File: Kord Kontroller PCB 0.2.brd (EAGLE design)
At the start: 242.5 x 100 mm, 188 parts, among them IC2 74HCT1G125DBV, J1 MIDIOUTB, J2 MIDIOUTA, J3 FTSH-105-01-L-DV-KJ, SW2 SPST_TACT-KMR2, U1 AP2112K-3.3, U2 ATSAMD51J19A-AUT, X3 microUSB

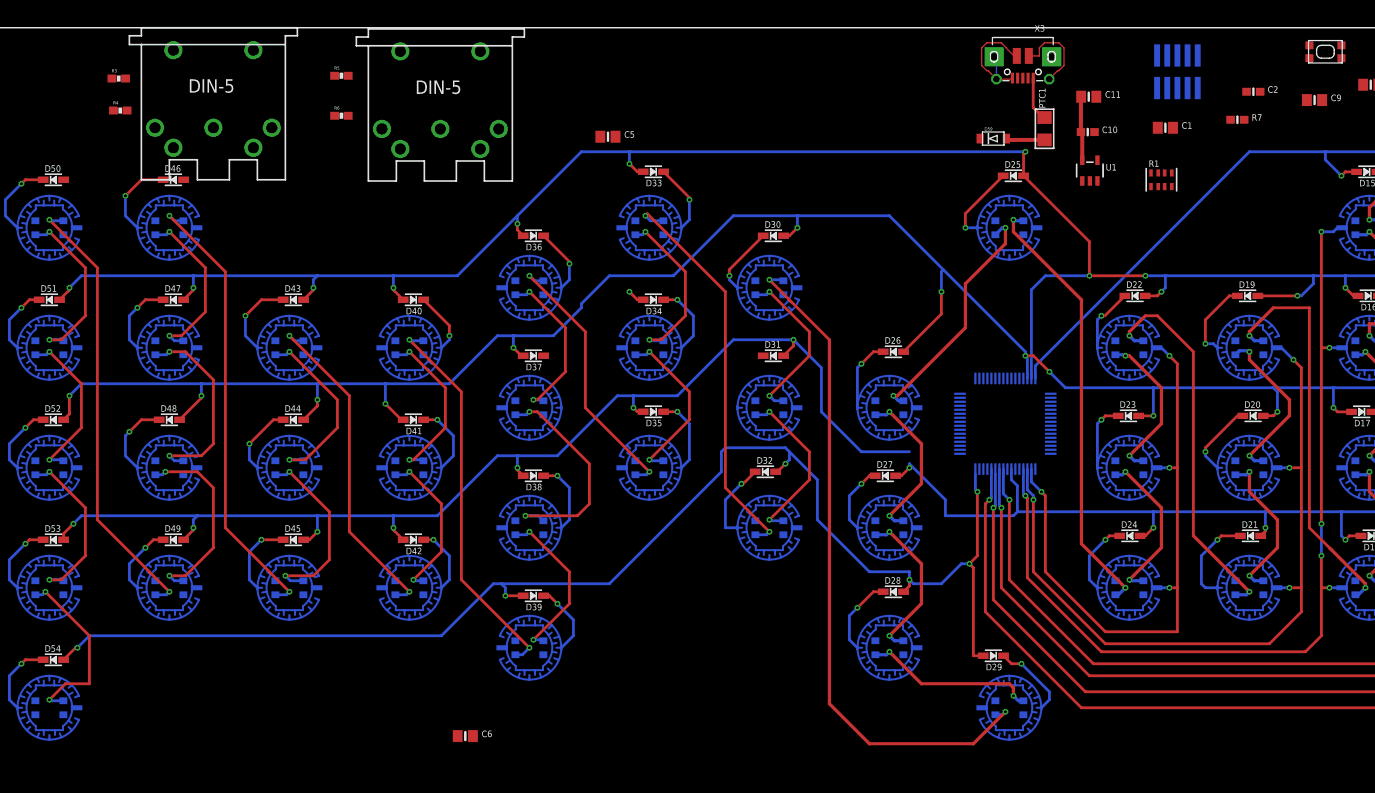
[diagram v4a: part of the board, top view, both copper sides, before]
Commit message: Added traces for 7-14
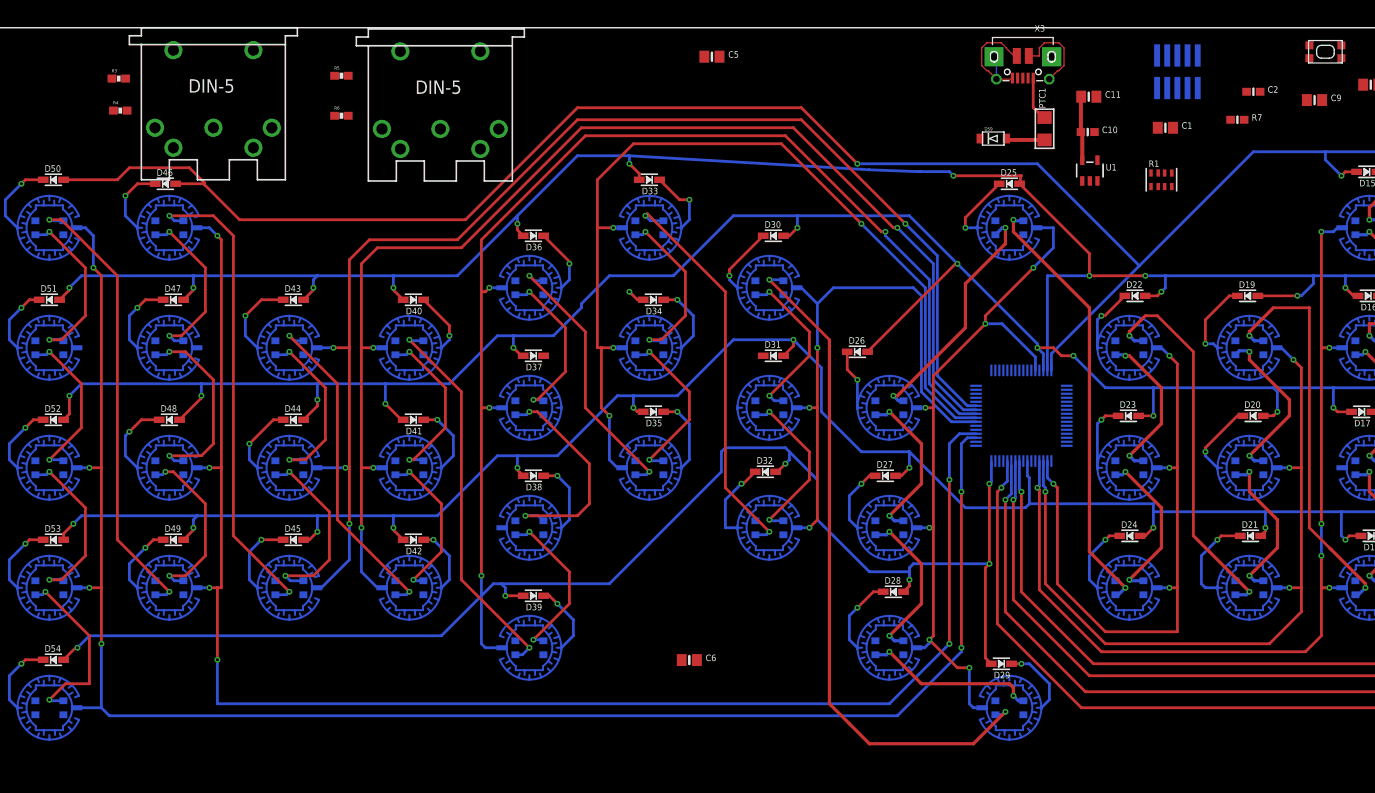
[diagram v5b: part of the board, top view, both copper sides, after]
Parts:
- moved C6 29.6 mm to (87.5, 21.0)
- moved C5 16.4 mm to (90.3, 96.4)
- moved D26 4.50 mm to (108.5, 59.5)
- moved U2 2.24 mm to (129.0, 51.5)
- moved D29 1.41 mm to (126.5, 20.5)
- moved D25 1.12 mm to (127.5, 80.5)
- moved D33 1.12 mm to (82.5, 81.0)
- moved D46 1.12 mm to (22.0, 80.5)
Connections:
- net COL10: now also U2.41; no longer U2.38
- net COL11: now also U2.42; no longer U2.41
- net COL12: now also U2.37, U2.43; no longer U2.42
- net COL13: now also U2.36; no longer U2.43
- net COL14: now also U2.35; no longer U2.44
- net COL7: now also B29.P$1, U2.60; no longer U2.35
- net COL8: now also U2.39; no longer B29.P$1, U2.36
- net COL9: now also U2.40; no longer U2.37
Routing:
- net COL14: track 0.00 -> 210.0 mm, vias 0 -> 6
- net COL13: track 0.00 -> 190.8 mm, vias 0 -> 6
- net COL12: track 0.00 -> 159.8 mm, vias 0 -> 4
- net COL11: track 0.00 -> 153.5 mm, vias 0 -> 4
- net ROW0: track 104.2 -> 257.7 mm, vias 3 -> 4
- net COL10: track 0.00 -> 148.2 mm, vias 0 -> 4
- net COL9: track 0.00 -> 113.7 mm, vias 0 -> 4
- net COL7: track 0.00 -> 88.3 mm, vias 0 -> 6
- net COL8: track 0.00 -> 70.1 mm, vias 0 -> 3
- net ROW1: track 312.9 -> 308.1 mm
- net ROW4: track 171.1 -> 175.2 mm
- net ROW2: track 316.4 -> 320.2 mm
- net N$100: track 57.1 -> 60.3 mm
- net N$112: track 24.7 -> 22.1 mm
- net N$81: track 9.06 -> 7.53 mm
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
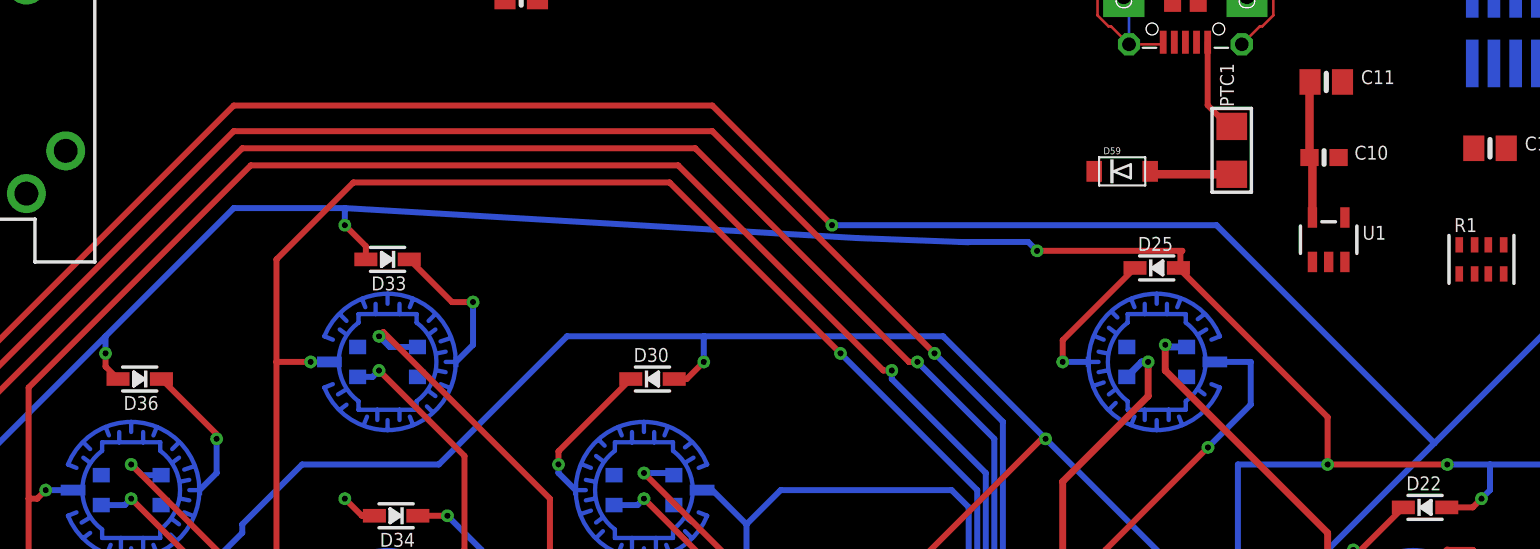
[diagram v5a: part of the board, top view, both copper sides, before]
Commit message: added last top button diodes
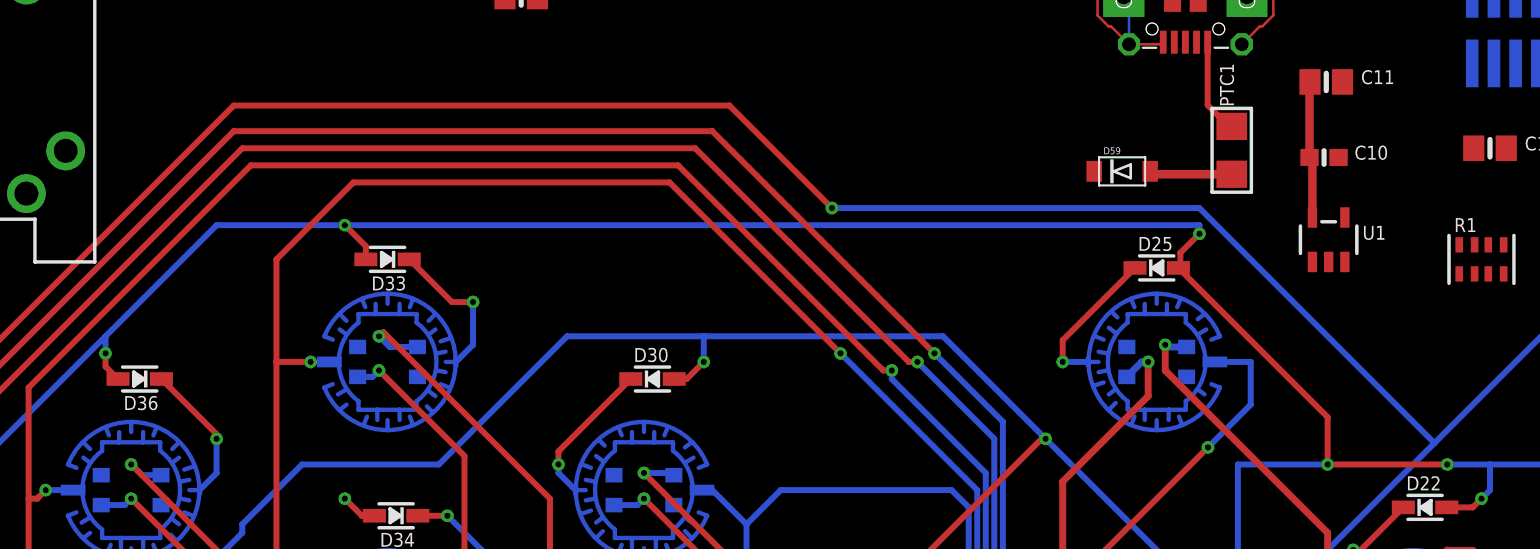
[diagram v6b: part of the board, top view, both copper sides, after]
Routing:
- net ROW1: track 308.1 -> 308.8 mm
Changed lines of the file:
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@@
 <wire x1="41" y1="69" x2="25.5" y2="69" width="0.35" layer="16"/>
 <wire x1="25.5" y1="69" x2="11.5" y2="69" width="0.35" layer="16"/>
-<wire x1="73.5" y1="84" x2="80" y2="84" width="0.35" layer="16"/>
-<wire x1="80" y1="84" x2="109.986528125" y2="82.2458375" width="0.35" layer="16"/>
-<wire x1="109.986528125" y1="82.2458375" x2="116.0007125" y2="82.01884375" width="0.35" layer="16"/>
-<wire x1="116.0007125" y1="82.01884375" x2="116.5" y2="82" width="0.35" layer="16"/>
+<wire x1="80" y1="83" x2="72.5" y2="83" width="0.35" layer="16"/>
+<wire x1="130" y1="82.5" x2="130" y2="83" width="0.35" layer="16"/>
+<wire x1="80" y1="83" x2="130" y2="83" width="0.35" layer="16"/>
 <wire x1="58.5" y1="69" x2="66" y2="76.5" width="0.35" layer="16"/>
 <via x="10" y="67.5" extent="1-16" drill="0.35"/>
-<wire x1="66" y1="76.5" x2="73.5" y2="84" width="0.35" layer="16"/>
+<wire x1="66" y1="76.5" x2="72.5" y2="83" width="0.35" layer="16"/>
 <wire x1="10" y1="67.5" x2="10" y2="67.23" width="0.35" layer="1"/>
 <wire x1="10" y1="67.23" x2="8.77" y2="66" width="0.35" layer="1"/>
@@
 <wire x1="81.23" y1="81.77" x2="80" y2="83" width="0.35" layer="1"/>
 <via x="80" y="83" extent="1-16" drill="0.35"/>
-<wire x1="80" y1="83" x2="80" y2="84" width="0.35" layer="16"/>
 <wire x1="171.09" y1="66.49" x2="170.51" y2="66.49" width="0.35" layer="1"/>
 <wire x1="170.51" y1="66.49" x2="169.5" y2="67.5" width="0.35" layer="1"/>
 <via x="169.5" y="67.5" extent="1-16" drill="0.35"/>
 <wire x1="169.5" y1="67.5" x2="169.5" y2="69" width="0.35" layer="16"/>
-<wire x1="128.885" y1="81.385" x2="129" y2="81.5" width="0.35" layer="1"/>
+<wire x1="128.885" y1="81.385" x2="130" y2="82.5" width="0.35" layer="1"/>
 <wire x1="128.885" y1="81.385" x2="128.885" y2="80.385" width="0.35" layer="1"/>
-<wire x1="129" y1="81.5" x2="120.5" y2="81.5" width="0.35" layer="1"/>
-<via x="120.5" y="81.5" extent="1-16" drill="0.35"/>
-<wire x1="120.5" y1="81.5" x2="119.98115625" y2="82.01884375" width="0.35" layer="16"/>
-<wire x1="119.98115625" y1="82.01884375" x2="116.0007125" y2="82.01884375" width="0.35" layer="16"/>
+<via x="130" y="82.5" extent="1-16" drill="0.35"/>
 </signal>
 <signal name="ROW2">
@@
 <wire x1="170.91" y1="81.99" x2="169.49" y2="81.99" width="0.35" layer="1"/>
 <wire x1="169" y1="81.5" x2="169.49" y2="81.99" width="0.35" layer="1"/>
-<wire x1="143.75" y1="70.25" x2="131" y2="83" width="0.35" layer="16"/>
-<via x="108.5" y="83" extent="1-16" drill="0.35"/>
-<wire x1="108.5" y1="83" x2="101.5" y2="90" width="0.35" layer="1"/>
-<wire x1="101.5" y1="90" x2="73.5" y2="90" width="0.35" layer="1"/>
+<wire x1="143.75" y1="70.25" x2="130" y2="84" width="0.35" layer="16"/>
+<via x="108.5" y="84" extent="1-16" drill="0.35"/>
+<wire x1="108.5" y1="84" x2="102.5" y2="90" width="0.35" layer="1"/>
+<wire x1="102.5" y1="90" x2="73.5" y2="90" width="0.35" layer="1"/>
 <wire x1="73.5" y1="90" x2="59.5" y2="76" width="0.35" layer="1"/>
 <wire x1="31.27" y1="76" x2="26.885" y2="80.385" width="0.35" layer="1"/>
 <wire x1="26.885" y1="80.385" x2="26.77" y2="80.5" width="0.35" layer="1"/>
 <wire x1="26.77" y1="80.5" x2="23.27" y2="80.5" width="0.35" layer="1"/>
-<wire x1="131" y1="83" x2="108.5" y2="83" width="0.35" layer="16"/>
+<wire x1="130" y1="84" x2="108.5" y2="84" width="0.35" layer="16"/>
 <wire x1="59.5" y1="76" x2="31.27" y2="76" width="0.35" layer="1"/>
 <wire x1="9.27" y1="81" x2="16" y2="81" width="0.35" layer="1"/>
@@
 <via x="113.5" y="75" extent="1-16" drill="0.35"/>
 <wire x1="113.5" y1="75" x2="113" y2="75" width="0.35" layer="1"/>
-<wire x1="113" y1="75" x2="100.5" y2="87.5" width="0.35" layer="1"/>
+<wire x1="113" y1="75" x2="106" y2="82" width="0.35" layer="1"/>
+<wire x1="106" y1="82" x2="100.5" y2="87.5" width="0.35" layer="1"/>
 <wire x1="59" y1="72.5" x2="48.5" y2="72.5" width="0.35" layer="1"/>
 <wire x1="48.5" y1="72.5" x2="46.5" y2="70.5" width="0.35" layer="1"/>

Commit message: routed power and midi
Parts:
- moved R4 217.1 mm to (233.4, 84.2), turned to 180 degrees
- moved R3 191.2 mm to (207.2, 84.2)
- moved J2 163.5 mm to (219.9, 100.3)
- moved J1 161.5 mm to (189.5, 100.0)
- moved R6 157.1 mm to (201.0, 84.5), turned to 180 degrees
- moved R5 134.3 mm to (178.0, 84.5)
- moved C6 99.6 mm to (165.0, 83.5)
- moved C3 90.0 mm to (158.8, 87.6)
- moved C5 69.7 mm to (158.8, 83.4)
- moved IC2 24.2 mm to (224.2, 73.9)
- moved R1 13.1 mm to (141.8, 93.2)
- moved U1 12.8 mm to (137.3, 94.9), turned to 180 degrees
- moved R7 11.0 mm to (146.0, 93.0), turned to 90 degrees
- moved C4 9.57 mm to (164.7, 87.6)
- moved C1 9.45 mm to (139.5, 81.8), turned to 180 degrees
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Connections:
- net D+: now also U2.45; no longer U2.46
- net D-: now also U2.46; no longer U2.45
- net MIDIOUTA: now also U2.50; no longer U2.29
- net MIDIOUTB: now also U2.49; no longer U2.30
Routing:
- net MIDIOUTA: track 0.00 -> 140.1 mm, vias 0 -> 5
- net LEVELSHIFT_3V: track 0.00 -> 128.9 mm, vias 0 -> 3
- net MIDIOUTB: track 0.00 -> 110.0 mm, vias 0 -> 5
- net NRESET: track 0.00 -> 97.6 mm, vias 0 -> 8
- net 3.3V: track 8.01 -> 83.5 mm, vias 0 -> 8
- net SWDCLK: track 0.00 -> 59.3 mm, vias 0 -> 6
- net SWDIO: track 0.00 -> 53.6 mm, vias 0 -> 6
- net D+: track 0.00 -> 53.2 mm, vias 0 -> 1
- net D-: track 0.00 -> 52.2 mm, vias 0 -> 1
- net SWO: track 0.00 -> 50.8 mm, vias 0 -> 6
- net VDDCORE1: track 0.00 -> 47.5 mm, vias 0 -> 7
- net VSW: track 0.00 -> 38.1 mm, vias 0 -> 5
- net LEVELSHIFT_5V: track 65.3 -> 91.8 mm
- net GND: track 26.3 -> 1.21 mm
- net VDD: track 0.00 -> 23.6 mm
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
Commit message: Finished Routinggit status
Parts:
- moved B12 15.0 mm to (187.5, 52.5)
- moved B13 15.0 mm to (187.5, 37.5)
- moved PTC1 9.25 mm to (119.9, 88.4)
- moved D59 1.82 mm to (131.2, 83.4)
- moved C1 1.50 mm to (139.5, 83.2)
- moved C10 1.00 mm to (137.8, 89.7)
- moved U1 1.00 mm to (137.3, 93.9)
- flipped X3 to the bottom
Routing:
- net GND: track 1.21 -> 364.7 mm, vias 0 -> 122
- net VDD: track 23.6 -> 104.1 mm, vias 0 -> 54
- net VSW: track 38.1 -> 0.00 mm, vias 5 -> 0
- net 3.3V: track 83.5 -> 109.3 mm
- net ROW3: track 318.5 -> 304.5 mm
- net N$84: track 0.00 -> 10.3 mm, vias 0 -> 1
- net VBUS: track 2.62 -> 12.1 mm
- net N$86: track 0.00 -> 9.27 mm, vias 0 -> 1
- net COL14: track 210.0 -> 213.6 mm, vias 6 -> 7
- net COL13: track 190.8 -> 194.2 mm, vias 6 -> 7
- net VDDCORE1: track 47.5 -> 50.8 mm
- net N$113: track 50.8 -> 47.6 mm
- net N$66: track 5.08 -> 8.21 mm, vias 0 -> 1
- net N$51: track 23.8 -> 21.0 mm
- net ROW2: track 322.9 -> 325.8 mm
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- added copper zone on layer 16, net GND
- added copper zone on layer 1, net VDD
- removed copper zone on layer 1, net GND
- removed copper zone on layer 16, net VDD
